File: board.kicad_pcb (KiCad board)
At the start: 6 copper layers, 197 x 134 mm, 26 parts, among them U1 MC68060RC50, U2 XC95144XL-5TQG100C, U3 SST39VF1601C-70-4C-EKE, U4 IS61WV51216BLL-10TLI, U5 IS61WV51216BLL-10TLI, U6 SST39VF1601C-70-4C-EKE

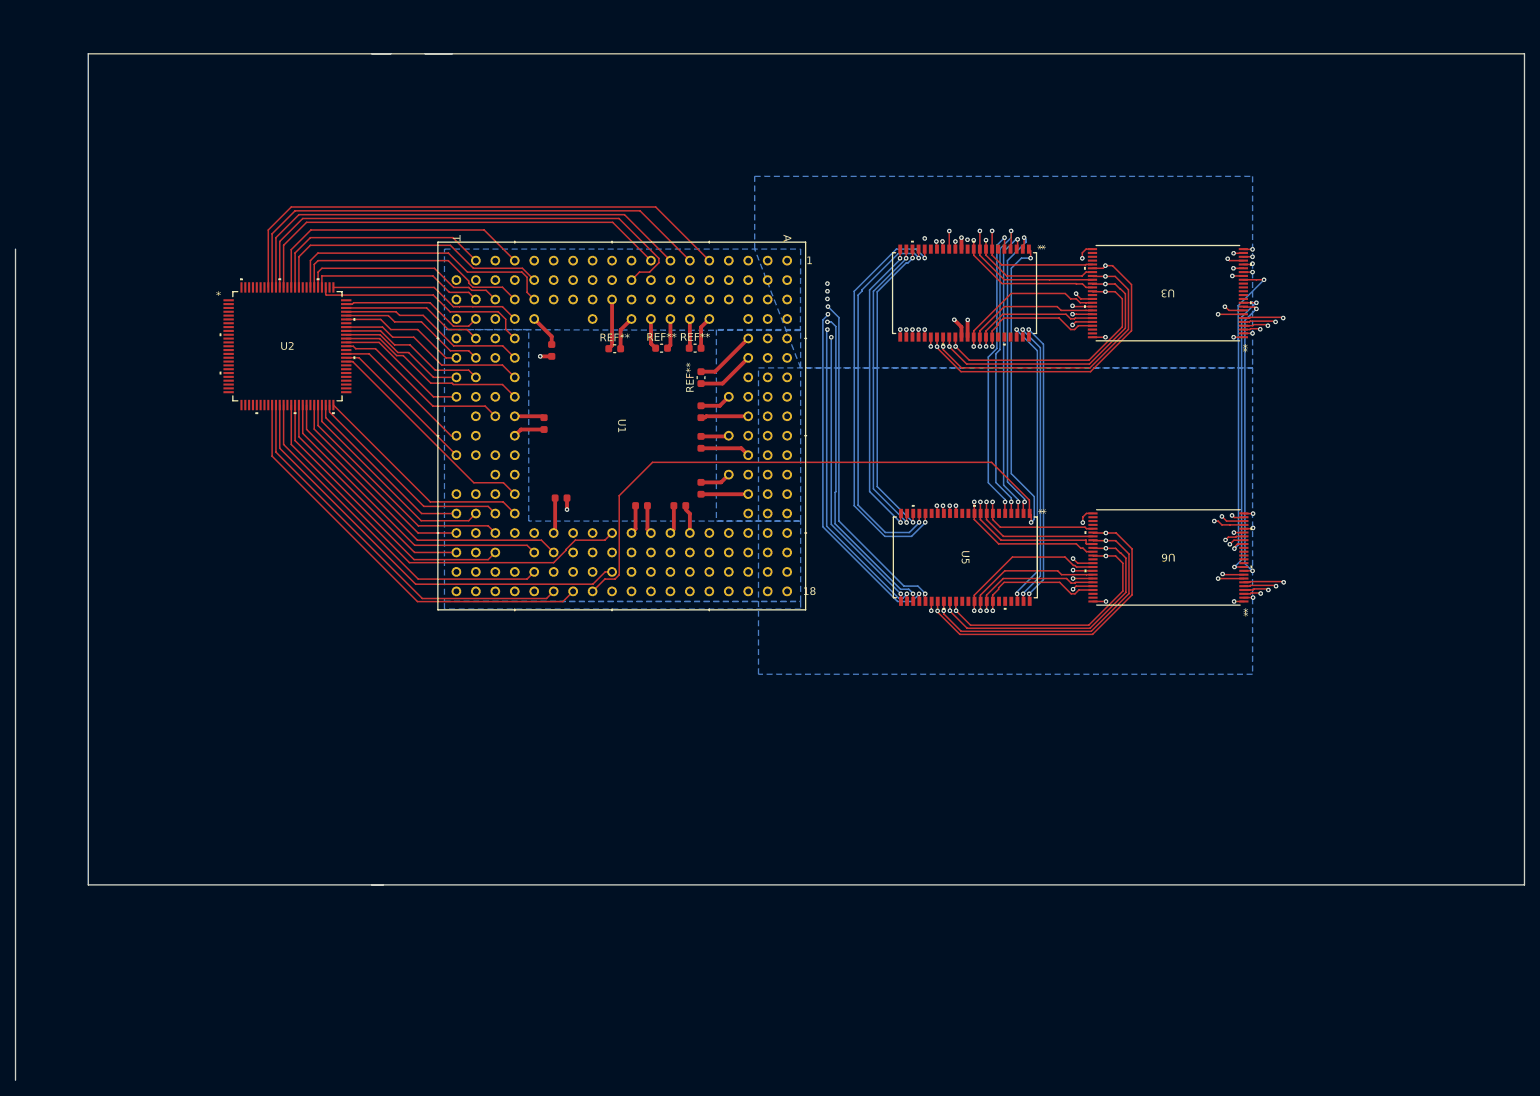
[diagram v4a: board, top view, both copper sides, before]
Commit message: Added buffers and re-rationalised traces
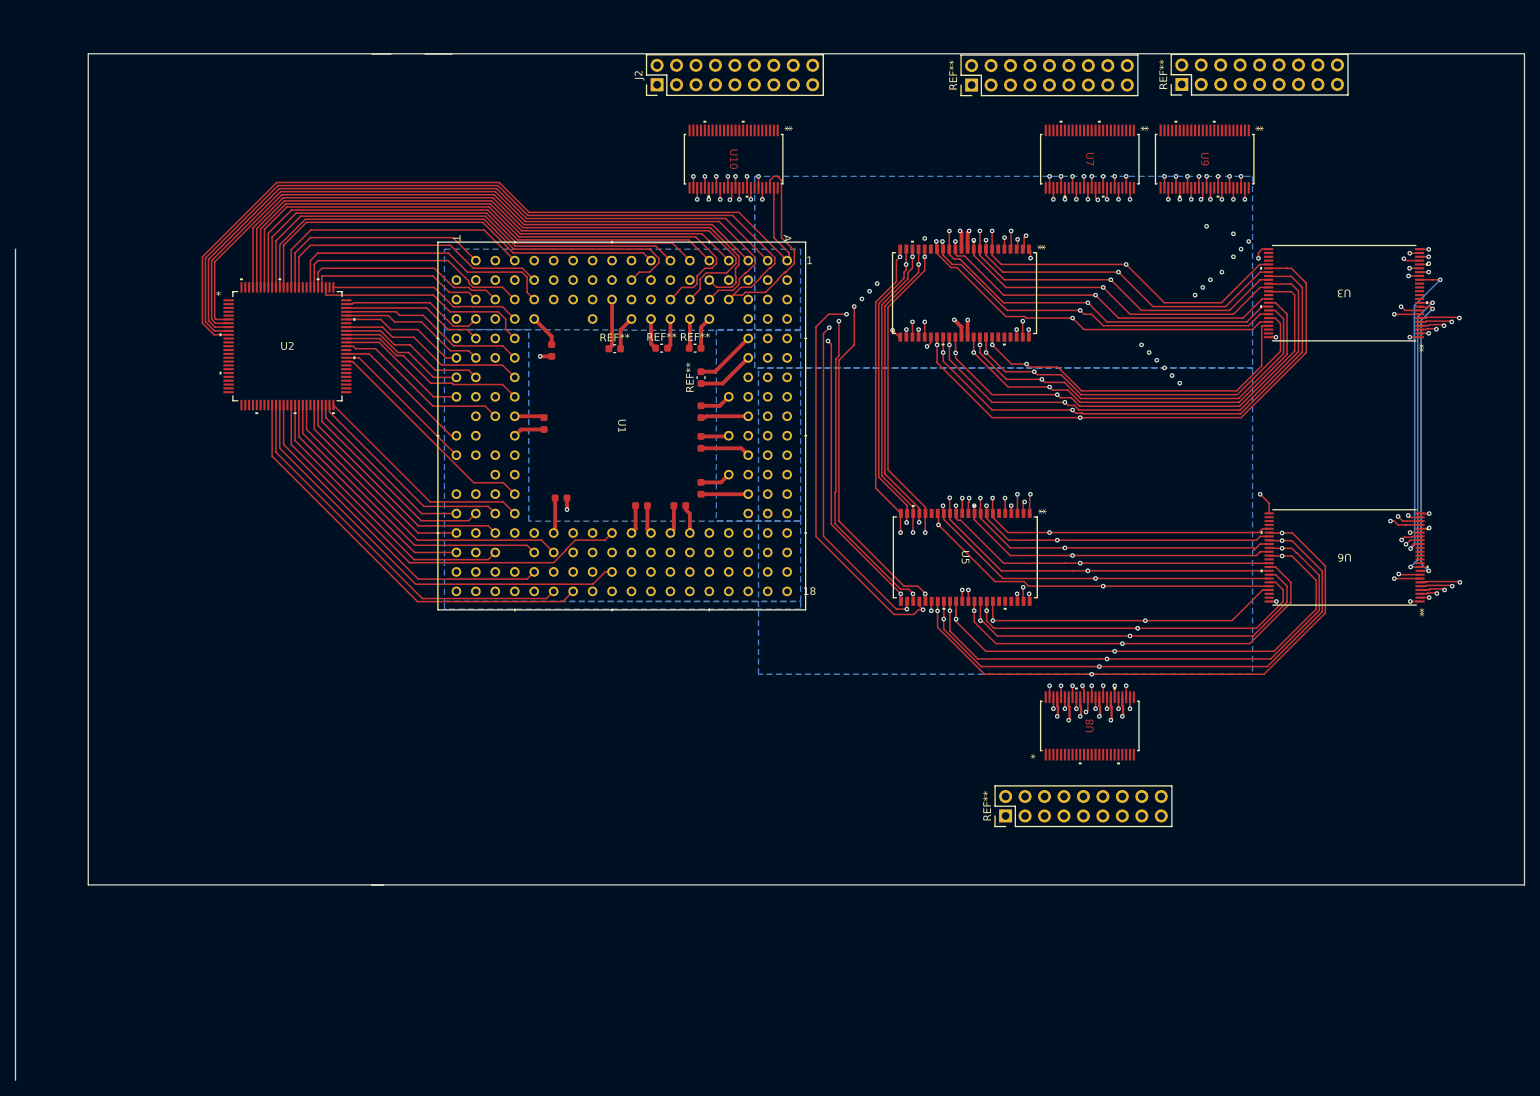
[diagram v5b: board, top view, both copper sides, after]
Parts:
- added J2: PinHeader_2x09_P2.54mm_Vertical, Connector_PinHeader_2.54mm:PinHeader_2x09_P2.54mm_Vertical, F.Cu at (92.3, 33.0)
- added REF**: PinHeader_2x09_P2.54mm_Vertical, Connector_PinHeader_2.54mm:PinHeader_2x09_P2.54mm_Vertical, F.Cu at (160.8, 33.0)
- added REF**: PinHeader_2x09_P2.54mm_Vertical, Connector_PinHeader_2.54mm:PinHeader_2x09_P2.54mm_Vertical, F.Cu at (133.3, 33.1)
- added REF**: PinHeader_2x09_P2.54mm_Vertical, Connector_PinHeader_2.54mm:PinHeader_2x09_P2.54mm_Vertical, F.Cu at (137.8, 128.5)
- added U10: SOT362-1_NEX, 74 buffer:SOT362-1_NEX, F.Cu at (102.2, 42.8)
- added U7: SOT362-1_NEX, 74 buffer:SOT362-1_NEX, F.Cu at (148.7, 42.8)
- added U8: SOT362-1_NEX, 74 buffer:SOT362-1_NEX, F.Cu at (148.8, 116.7)
- added U9: SOT362-1_NEX, 74 buffer:SOT362-1_NEX, F.Cu at (163.7, 42.8)
- moved U3 23.0 mm to (181.9, 60.2)
- moved U6 23.0 mm to (182.0, 94.7)
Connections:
- U1 pad M1: unconnected-(U1A-A13-PadM1) -> /A13
- U2 pad 10: unconnected-(U2-IO-Pad10) -> /A31
- U2 pad 6: unconnected-(U2-IO-Pad6) -> /A27
- U2 pad 7: unconnected-(U2-IO-Pad7) -> /A28
- U2 pad 8: unconnected-(U2-IO-Pad8) -> /A29
- U2 pad 9: unconnected-(U2-IO-Pad9) -> /A30
- U2 pad 94: unconnected-(U2-IO-Pad94) -> /A23
- U2 pad 95: unconnected-(U2-IO-Pad95) -> /A24
- U2 pad 96: unconnected-(U2-IO-Pad96) -> /A25
- U2 pad 97: unconnected-(U2-IO-Pad97) -> /A26
- U3 pad 10: /A20 -> unconnected-(U3-NC-Pad10)
- U3 pad 37: unconnected-(U3-VDD-Pad37) -> /VCC
- U4 pad 11: unconnected-(U4-VDD-Pad11) -> /VCC
- U5 pad 11: unconnected-(U5-VDD-Pad11) -> /VCC
- U5 pad 12: unconnected-(U5-GND-Pad12) -> /GND
- U5 pad 29: /D31 -> /D24
- U5 pad 30: /D30 -> /D25
- U5 pad 31: /D29 -> /D26
- U5 pad 32: /D28 -> /D27
- U5 pad 33: unconnected-(U5-VDD-Pad33) -> /VCC
- U5 pad 34: unconnected-(U5-GND-Pad34) -> /GND
- U5 pad 35: /D27 -> /D28
- U5 pad 36: /D26 -> /D29
- U5 pad 37: /D25 -> /D30
- U5 pad 38: /D24 -> /D31
- U6 pad 10: /A20 -> unconnected-(U6-NC-Pad10)
- U6 pad 37: /D27 -> /VCC
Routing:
- net /A30: track 0.00 -> 127.9 mm
- net /A28: track 0.00 -> 120.2 mm, vias 0 -> 1
- net /A31: track 0.00 -> 107.7 mm
- net /A26: track 0.00 -> 104.5 mm, vias 0 -> 1
- net /A25: track 0.00 -> 103.8 mm, vias 0 -> 1
- net /A29: track 0.00 -> 101.5 mm, vias 0 -> 1
- net /A23: track 0.00 -> 99.3 mm, vias 0 -> 1
- net /A27: track 0.00 -> 95.7 mm, vias 0 -> 1
- net /A24: track 0.00 -> 86.0 mm, vias 0 -> 1
- net /A13: track 207.8 -> 289.5 mm, vias 5 -> 7
- net /A11: track 213.3 -> 292.7 mm, vias 5 -> 7
- net /A10: track 224.3 -> 301.7 mm, vias 5 -> 7
- net /A12: track 212.0 -> 287.6 mm, vias 5 -> 7
- net /A14: track 196.9 -> 271.3 mm, vias 5 -> 7
- net /A15: track 169.7 -> 241.4 mm, vias 5 -> 7
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
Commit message: Added jumpers for expansion board and more address lines to the CPLD
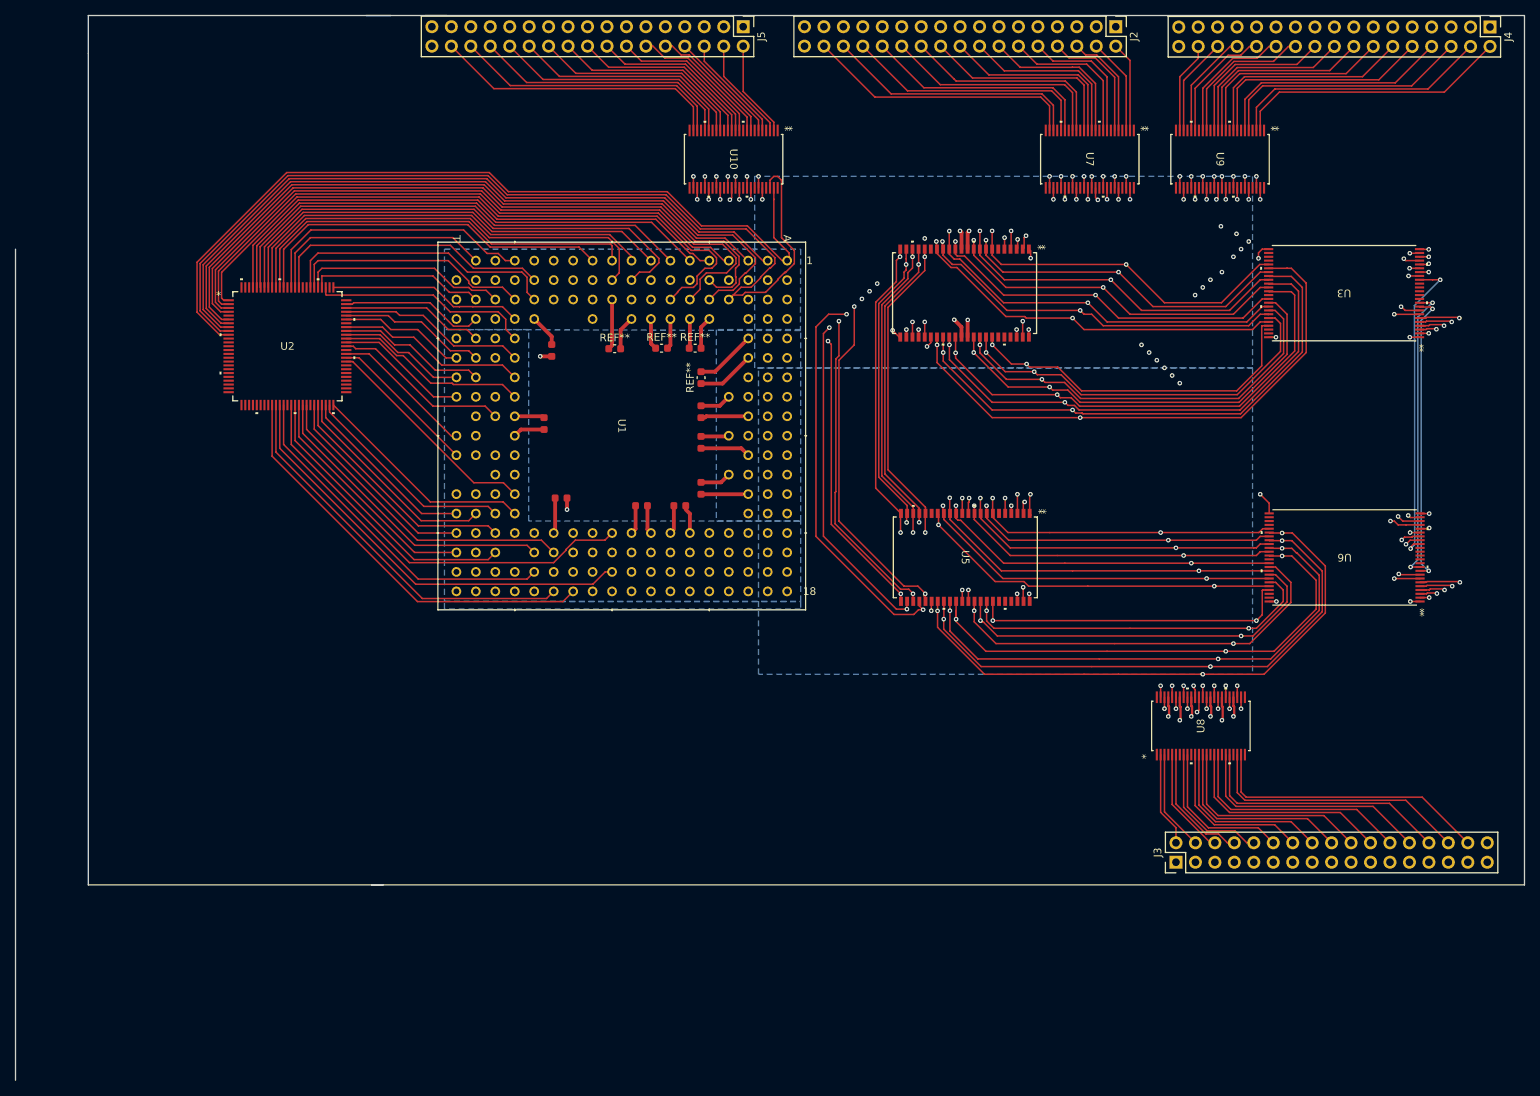
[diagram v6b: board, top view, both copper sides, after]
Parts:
- removed the REF** at (160.8, 33.0)
- removed the REF** at (133.3, 33.1)
- removed the REF** at (137.8, 128.5)
- added J3: Conn_2Rows-33Pins, Connector_PinHeader_2.54mm:PinHeader_2x17_P2.54mm_Vertical, F.Cu at (160.0, 134.5)
- added J4: Conn_2Rows-33Pins, Connector_PinHeader_2.54mm:PinHeader_2x17_P2.54mm_Vertical, F.Cu at (201.0, 25.5)
- added J5: Conn_2Rows-33Pins, Connector_PinHeader_2.54mm:PinHeader_2x17_P2.54mm_Vertical, F.Cu at (103.5, 25.5)
- J2: value PinHeader_2x09_P2.54mm_Vertical -> Conn_2Rows-33Pins; footprint Connector_PinHeader_2.54mm:PinHeader_2x09_P2.54mm_Vertical -> Connector_PinHeader_2.54mm:PinHeader_2x17_P2.54mm_Vertical
- U10, U7, U8, U9: value SOT362-1_NEX -> 74LVC162245ADGG
- moved J2 60.4 mm to (152.1, 25.5), turned to -90 degrees
- moved U8 14.5 mm to (163.3, 116.7)
- moved U9 2.00 mm to (165.7, 42.8)
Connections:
- J2 pad 1: (no net) -> /GND
- J2 pad 10: (no net) -> /EXT_D4
- J2 pad 11: (no net) -> /GND
- J2 pad 12: (no net) -> /EXT_D5
- J2 pad 13: (no net) -> /GND
- J2 pad 14: (no net) -> /EXT_D6
- J2 pad 15: (no net) -> /GND
- J2 pad 16: (no net) -> /EXT_D7
- J2 pad 17: (no net) -> /GND
- J2 pad 18: (no net) -> /EXT_D8
- J2 pad 2: (no net) -> /EXT_D0
- J2 pad 3: (no net) -> /GND
- J2 pad 4: (no net) -> /EXT_D1
- J2 pad 5: (no net) -> /GND
- J2 pad 6: (no net) -> /EXT_D2
- J2 pad 7: (no net) -> /GND
- J2 pad 8: (no net) -> /EXT_D3
- J2 pad 9: (no net) -> /GND
- U1 pad M1: /A13 -> unconnected-(U1A-A13-PadM1)
- U10 pad 1: (no net) -> unconnected-(U10-1DIR-Pad1)
- U10 pad 10: (no net) -> unconnected-(U10-GND-Pad10)
- U10 pad 11: (no net) -> /EXT_A25
- U10 pad 12: (no net) -> /EXT_A24
- U10 pad 13: (no net) -> /EXT_A23
- U10 pad 14: (no net) -> /EXT_A22
- U10 pad 15: (no net) -> unconnected-(U10-GND-Pad15)
- U10 pad 16: (no net) -> /EXT_A21
- U10 pad 17: (no net) -> /EXT_A20
- U10 pad 18: (no net) -> unconnected-(U10-VCC-Pad18)
- U10 pad 19: (no net) -> /EXT_A19
- U10 pad 2: (no net) -> /EXT_A31
- U10 pad 20: (no net) -> /EXT_A18
- U10 pad 21: (no net) -> unconnected-(U10-GND-Pad21)
- U10 pad 22: (no net) -> /EXT_A17
- U10 pad 23: (no net) -> /EXT_A16
- U10 pad 24: (no net) -> unconnected-(U10-2DIR-Pad24)
- U10 pad 25: (no net) -> unconnected-(U10-2OE*-Pad25)
- U10 pad 28: (no net) -> unconnected-(U10-GND-Pad28)
- U10 pad 3: (no net) -> /EXT_A30
- U10 pad 31: (no net) -> unconnected-(U10-VCC-Pad31)
- U10 pad 34: (no net) -> unconnected-(U10-GND-Pad34)
- U10 pad 39: (no net) -> unconnected-(U10-GND-Pad39)
- U10 pad 4: (no net) -> unconnected-(U10-GND-Pad4)
- U10 pad 42: (no net) -> unconnected-(U10-VCC-Pad42)
- U10 pad 45: (no net) -> unconnected-(U10-GND-Pad45)
- U10 pad 48: (no net) -> unconnected-(U10-1OE*-Pad48)
- U10 pad 5: (no net) -> /EXT_A29
- U10 pad 6: (no net) -> /EXT_A28
- U10 pad 7: (no net) -> unconnected-(U10-VCC-Pad7)
- U10 pad 8: (no net) -> /EXT_A27
- U10 pad 9: (no net) -> /EXT_A26
- U2 pad 1: unconnected-(U2-I/O/GTS3-Pad1) -> /A23
- U2 pad 100: unconnected-(U2-GND-Pad100) -> /GND
- U2 pad 2: unconnected-(U2-I/O/GTS4-Pad2) -> /A24
- U2 pad 21: unconnected-(U2-GND-Pad21) -> /GND
- U2 pad 26: unconnected-(U2-VCCIO2.5V/3.3V-Pad26) -> /VCC
- U2 pad 3: unconnected-(U2-I/O/GTS1-Pad3) -> /A25
- U2 pad 31: unconnected-(U2-GND-Pad31) -> /GND
- U2 pad 38: unconnected-(U2-VCCIO2.5V/3.3V-Pad38) -> /VCC
- U2 pad 4: unconnected-(U2-I/O/GTS2-Pad4) -> /A26
- U2 pad 44: unconnected-(U2-GND-Pad44) -> /GND
- U2 pad 5: unconnected-(U2-VCCINT3.3V-Pad5) -> /VCC
- U2 pad 51: unconnected-(U2-VCCIO2.5V/3.3V-Pad51) -> /VCC
- U2 pad 57: unconnected-(U2-VCCINT3.3V-Pad57) -> /VCC
- U2 pad 62: unconnected-(U2-GND-Pad62) -> /GND
- U2 pad 69: unconnected-(U2-GND-Pad69) -> /GND
- U2 pad 75: unconnected-(U2-GND-Pad75) -> /GND
- U2 pad 84: unconnected-(U2-GND-Pad84) -> /GND
- U2 pad 88: unconnected-(U2-VCCIO2.5V/3.3V-Pad88) -> /VCC
- U2 pad 89: /A18 -> /A14
- U2 pad 90: /A19 -> /A15
- U2 pad 91: /A20 -> /A16
- U2 pad 92: /A21 -> /A17
- U2 pad 93: /A22 -> /A18
- U2 pad 94: /A23 -> /A19
- U2 pad 95: /A24 -> /A20
- U2 pad 96: /A25 -> /A21
- U2 pad 97: /A26 -> /A22
- U2 pad 98: unconnected-(U2-VCCINT3.3V-Pad98) -> /VCC
- U3 pad 37: /VCC -> unconnected-(U3-VDD-Pad37)
- U4 pad 11: /VCC -> unconnected-(U4-VDD-Pad11)
- U4 pad 12: /GND -> unconnected-(U4-GND-Pad12)
- U4 pad 33: /VCC -> unconnected-(U4-VDD-Pad33)
- U4 pad 34: /GND -> unconnected-(U4-GND-Pad34)
- U5 pad 11: /VCC -> unconnected-(U5-VDD-Pad11)
- U5 pad 12: /GND -> unconnected-(U5-GND-Pad12)
- U5 pad 29: /D24 -> /D31
- U5 pad 30: /D25 -> /D30
- U5 pad 31: /D26 -> /D29
- U5 pad 32: /D27 -> /D28
- U5 pad 33: /VCC -> unconnected-(U5-VDD-Pad33)
- U5 pad 34: /GND -> unconnected-(U5-GND-Pad34)
- U5 pad 35: /D28 -> /D27
- U5 pad 36: /D29 -> /D26
- U5 pad 37: /D30 -> /D25
- U5 pad 38: /D31 -> /D24
- U6 pad 37: /VCC -> /D27
- U7 pad 1: (no net) -> unconnected-(U7-1DIR-Pad1)
- U7 pad 10: (no net) -> /GND
- U7 pad 11: (no net) -> /EXT_D6
- U7 pad 12: (no net) -> /EXT_D7
- U7 pad 13: (no net) -> /EXT_D8
- U7 pad 14: (no net) -> /EXT_D9
- U7 pad 15: (no net) -> /GND
- U7 pad 16: (no net) -> /EXT_D10
- U7 pad 17: (no net) -> /EXT_D11
- U7 pad 18: (no net) -> /VCC
- U7 pad 19: (no net) -> /EXT_D12
- U7 pad 2: (no net) -> /EXT_D0
- U7 pad 20: (no net) -> /EXT_D13
- U7 pad 21: (no net) -> /GND
- U7 pad 22: (no net) -> /EXT_D14
- U7 pad 23: (no net) -> /EXT_D15
- U7 pad 24: (no net) -> unconnected-(U7-2DIR-Pad24)
- U7 pad 25: (no net) -> unconnected-(U7-2OE*-Pad25)
- U7 pad 28: (no net) -> /GND
- U7 pad 3: (no net) -> /EXT_D1
- U7 pad 31: (no net) -> /VCC
- U7 pad 34: (no net) -> /GND
- U7 pad 39: (no net) -> /GND
- U7 pad 4: (no net) -> /GND
- U7 pad 42: (no net) -> /VCC
- U7 pad 45: (no net) -> /GND
- U7 pad 48: (no net) -> unconnected-(U7-1OE*-Pad48)
- U7 pad 5: (no net) -> /EXT_D2
- U7 pad 6: (no net) -> /EXT_D3
- U7 pad 7: (no net) -> /VCC
- U7 pad 8: (no net) -> /EXT_D4
- U7 pad 9: (no net) -> /EXT_D5
- U8 pad 1: (no net) -> unconnected-(U8-1DIR-Pad1)
- U8 pad 10: (no net) -> /GND
- U8 pad 11: (no net) -> /EXT_D22
- U8 pad 12: (no net) -> /EXT_D23
- U8 pad 13: (no net) -> /EXT_D24
- U8 pad 14: (no net) -> /EXT_D25
- U8 pad 15: (no net) -> /GND
- U8 pad 16: (no net) -> /EXT_D26
- U8 pad 17: (no net) -> /EXT_D27
- U8 pad 18: (no net) -> /VCC
- U8 pad 19: (no net) -> /EXT_D28
- U8 pad 2: (no net) -> /EXT_D16
- U8 pad 20: (no net) -> /EXT_D29
- U8 pad 21: (no net) -> /GND
- U8 pad 22: (no net) -> /EXT_D30
- U8 pad 23: (no net) -> /EXT_D31
- U8 pad 24: (no net) -> unconnected-(U8-2DIR-Pad24)
- U8 pad 25: (no net) -> unconnected-(U8-2OE*-Pad25)
- U8 pad 3: (no net) -> /EXT_D17
- U8 pad 4: (no net) -> /GND
- U8 pad 48: (no net) -> unconnected-(U8-1OE*-Pad48)
- U8 pad 5: (no net) -> /EXT_D18
- U8 pad 6: (no net) -> /EXT_D19
- U8 pad 7: (no net) -> /VCC
- U8 pad 8: (no net) -> /EXT_D20
- U8 pad 9: (no net) -> /EXT_D21
- U9 pad 1: (no net) -> unconnected-(U9-1DIR-Pad1)
- U9 pad 10: (no net) -> /GND
- U9 pad 11: (no net) -> /EXT_A6
- U9 pad 12: (no net) -> /EXT_A7
- U9 pad 13: (no net) -> /EXT_A8
- U9 pad 14: (no net) -> /EXT_A9
- U9 pad 15: (no net) -> /GND
- U9 pad 16: (no net) -> /EXT_A10
- U9 pad 17: (no net) -> /EXT_A11
- U9 pad 18: (no net) -> /VCC
- U9 pad 19: (no net) -> /EXT_A12
- U9 pad 2: (no net) -> /EXT_A0
- U9 pad 20: (no net) -> /EXT_A13
- U9 pad 21: (no net) -> /GND
- U9 pad 22: (no net) -> /EXT_A14
- U9 pad 23: (no net) -> /EXT_A15
- U9 pad 24: (no net) -> unconnected-(U9-2DIR-Pad24)
- U9 pad 25: (no net) -> unconnected-(U9-2OE*-Pad25)
- U9 pad 28: (no net) -> /GND
- U9 pad 3: (no net) -> /EXT_A1
- U9 pad 31: (no net) -> /VCC
- U9 pad 34: (no net) -> /GND
- U9 pad 39: (no net) -> /GND
- U9 pad 4: (no net) -> /GND
- U9 pad 42: (no net) -> /VCC
- U9 pad 45: (no net) -> /GND
- U9 pad 48: (no net) -> unconnected-(U9-1OE*-Pad48)
- U9 pad 5: (no net) -> /EXT_A2
- U9 pad 6: (no net) -> /EXT_A3
- U9 pad 7: (no net) -> /VCC
- U9 pad 8: (no net) -> /EXT_A4
- U9 pad 9: (no net) -> /EXT_A5
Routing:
- net /A16: track 198.9 -> 256.6 mm
- net /A17: track 231.5 -> 288.1 mm
- net /A15: track 241.4 -> 295.4 mm
- net /A14: track 271.3 -> 320.7 mm
- net /EXT_A16: track 0.00 -> 38.0 mm
- net /EXT_D31: track 0.00 -> 37.2 mm
- net /EXT_A0: track 0.00 -> 36.0 mm
- net /EXT_A17: track 0.00 -> 36.0 mm
- net /EXT_D15: track 0.00 -> 35.9 mm
- net /EXT_D30: track 0.00 -> 35.2 mm
- net /EXT_A1: track 0.00 -> 34.3 mm
- net /EXT_A18: track 0.00 -> 34.2 mm
- net /EXT_D29: track 0.00 -> 33.9 mm
- net /EXT_D14: track 0.00 -> 33.9 mm
- net /EXT_A2: track 0.00 -> 33.3 mm
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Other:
- board size 197 x 134 mm -> 197 x 139 mm
